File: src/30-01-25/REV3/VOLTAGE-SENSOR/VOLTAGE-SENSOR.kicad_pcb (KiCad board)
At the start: 2 copper layers, 90 x 85 mm, 83 parts, among them U1 LM324, U2 zmpt101b, U6 zmpt101b, U7 LM324, U8 zmpt101b, U9 LM324

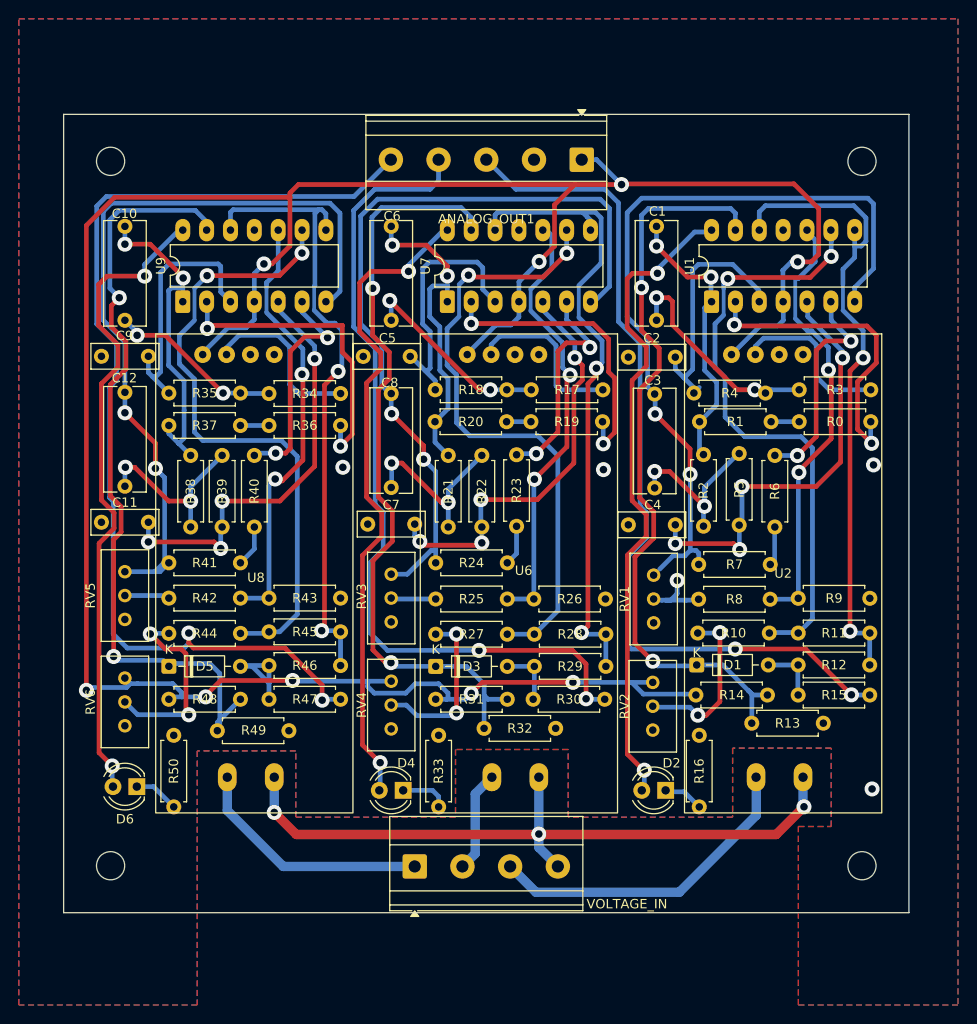
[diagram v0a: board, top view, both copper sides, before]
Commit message: Change: reading data by polling
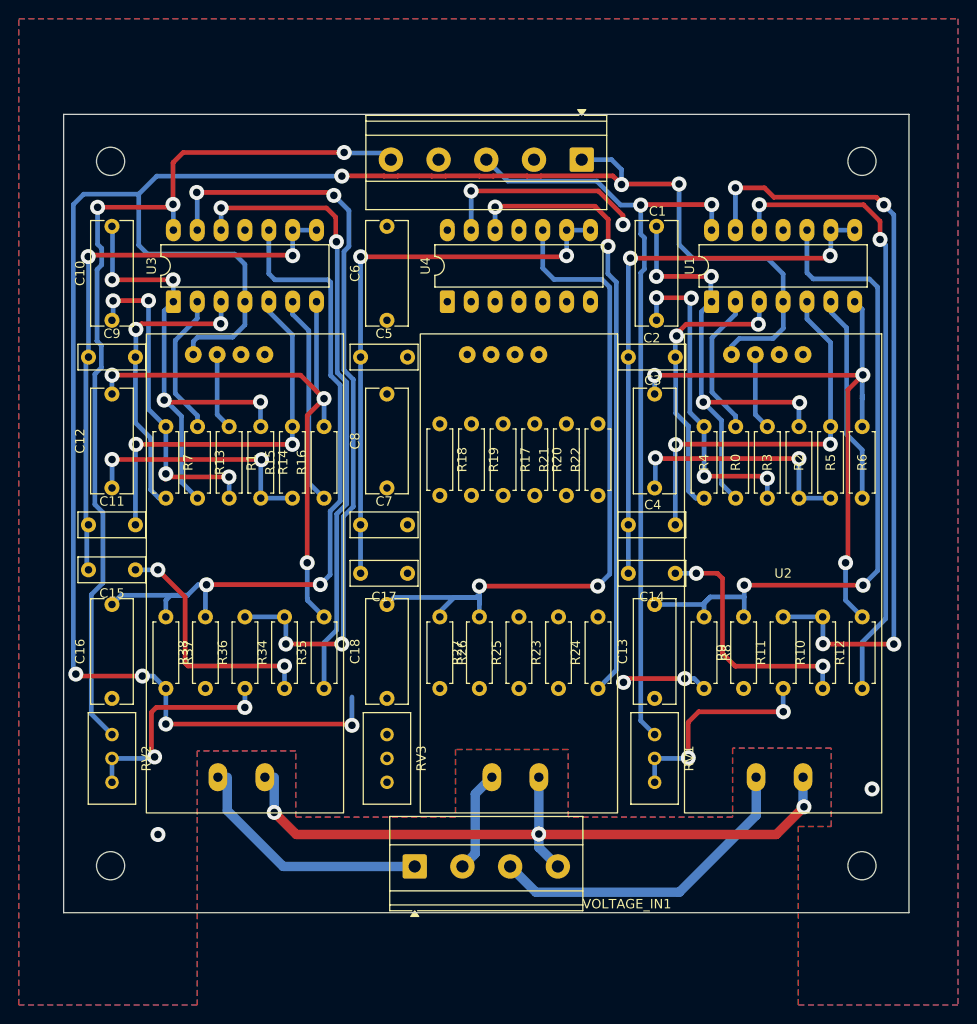
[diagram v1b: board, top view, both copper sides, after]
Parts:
- removed D1, D3, D5: 1N5711, Diode_THT:D_DO-35_SOD27_P7.62mm_Horizontal
- removed D2, D4, D6: LED, LED_THT:LED_D4.0mm
- removed R28, R29, R30, R39, R40, R41, R42, R43, R44, R45, R46, R47: 68k, Resistor_THT:R_Axial_DIN0207_L6.3mm_D2.5mm_P7.62mm_Horizontal
- removed R31, R48: 400, Resistor_THT:R_Axial_DIN0207_L6.3mm_D2.5mm_P7.62mm_Horizontal
- removed R32, R49: 420, Resistor_THT:R_Axial_DIN0207_L6.3mm_D2.5mm_P7.62mm_Horizontal
- removed R33, R50: 100, Resistor_THT:R_Axial_DIN0207_L6.3mm_D2.5mm_P7.62mm_Horizontal
- removed RV4, RV5, RV6: R_Potentiometer, Potentiometer_THT:Potentiometer_Bourns_3296W_Vertical
- removed U7, U9: LM324, Package_DIP:DIP-14_W7.62mm_LongPads
- added C13: 100nF, Capacitor_THT:C_Rect_L11.0mm_W4.3mm_P10.00mm_MKT, F.Cu at (157.7, 112.4)
- added C14: 1uF, Capacitor_THT:C_Rect_L7.0mm_W2.5mm_P5.00mm, F.Cu at (159.9, 99.0)
- added C15: 1uF, Capacitor_THT:C_Rect_L7.0mm_W2.5mm_P5.00mm, F.Cu at (102.4, 98.7)
- added C16: 100nF, Capacitor_THT:C_Rect_L11.0mm_W4.3mm_P10.00mm_MKT, F.Cu at (99.9, 112.4)
- added C17: 1uF, Capacitor_THT:C_Rect_L7.0mm_W2.5mm_P5.00mm, F.Cu at (131.4, 99.0)
- added C18: 100nF, Capacitor_THT:C_Rect_L11.0mm_W4.3mm_P10.00mm_MKT, F.Cu at (129.2, 112.4)
- added U3: LM324, Package_DIP:DIP-14_W7.62mm_LongPads, F.Cu at (106.5, 70.1)
- added U4: LM324, Package_DIP:DIP-14_W7.62mm_LongPads, F.Cu at (135.6, 70.1)
- R0, R19, R22, R6: value 68k -> 130k
- R10, R23, R34: value 68k -> 10k
- R11, R25, R36: value 68k -> 1k
- R12, R24, R35: value 68k -> 5.1k
- R13: value 420 -> 130k
- R14: value 400 -> 68k
- R16: value 100 -> 130k
- R26, R27, R37, R38, R8, R9: value 68k -> 100k
- RV1, RV2, RV3: value R_Potentiometer -> 10k
- moved R13 73.7 mm to (109.0, 83.4), turned to -90 degrees
- moved R7 66.0 mm to (105.7, 83.4), turned to -90 degrees
- moved R15 64.9 mm to (119.1, 91.0), turned to 90 degrees
- moved R14 61.0 mm to (115.8, 83.4), turned to -90 degrees
- moved RV2 58.5 mm to (99.9, 121.3), turned to -90 degrees
- moved R1 50.1 mm to (112.4, 83.4), turned to -90 degrees
- moved R16 47.3 mm to (122.5, 91.0), turned to 90 degrees
- moved R35 32.7 mm to (122.5, 111.3), turned to 90 degrees
- moved R34 32.0 mm to (118.3, 111.3), turned to 90 degrees
- moved R36 29.8 mm to (114.1, 111.3), turned to 90 degrees
- moved R23 25.3 mm to (147.5, 111.3), turned to 90 degrees
- moved R38 24.9 mm to (109.9, 111.3), turned to 90 degrees
- moved RV3 22.2 mm to (129.2, 121.3), turned to -90 degrees
- moved RV1 22.1 mm to (157.7, 121.3), turned to -90 degrees
- moved R37 20.4 mm to (105.7, 103.7), turned to -90 degrees
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- renumbered VOLTAGE_IN to VOLTAGE_IN1
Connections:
- C11 pad 1: GND -> VGND3
- C11 pad 2: Net-(U9B-+) -> Net-(U3B-+)
- C2 pad 1: GND -> VGND1
- C4 pad 1: GND -> VGND1
- C5 pad 1: GND -> VGND2
- C7 pad 1: GND -> VGND2
- C7 pad 2: Net-(U7B-+) -> Net-(U4B-+)
- C9 pad 1: GND -> VGND3
- C9 pad 2: Net-(U9A-+) -> Net-(U3A-+)
- R0 pad 2: Net-(R0-Pad2) -> Net-(C1-Pad2)
- R1 pad 1: Net-(C1-Pad2) -> OUT_S3
- R1 pad 2: Net-(R0-Pad2) -> Net-(C10-Pad1)
- R10 pad 1: Net-(R10-Pad1) -> Net-(C14-Pad1)
- R10 pad 2: Net-(U1C--) -> Net-(U1D--)
- R11 pad 1: Net-(U1D-+) -> Net-(R11-Pad1)
- R11 pad 2: Net-(U1C--) -> Net-(U1D--)
- R12 pad 1: Net-(D1-A) -> Net-(U1D-+)
- R12 pad 2: Net-(U1D-+) -> Net-(C3-Pad2)
- R13 pad 1: GND -> Net-(U3A--)
- R13 pad 2: Net-(D1-K) -> Net-(C10-Pad2)
- R14 pad 1: Net-(D1-K) -> Net-(C10-Pad2)
- R14 pad 2: 5V -> Net-(C12-Pad1)
- R15 pad 1: SIGNAL_OUT1 -> Net-(C12-Pad1)
- R15 pad 2: Net-(D1-A) -> Net-(U3B-+)
- R16 pad 1: GND -> Net-(U3B--)
- R16 pad 2: Net-(D2-K) -> Net-(C12-Pad2)
- R19 pad 2: Net-(R19-Pad2) -> Net-(C6-Pad2)
- R20 pad 2: Net-(R19-Pad2) -> Net-(C8-Pad1)
- R21 pad 1: Net-(C6-Pad2) -> Net-(C8-Pad1)
- R21 pad 2: Net-(C8-Pad1) -> Net-(U4B-+)
- R22 pad 1: Net-(C8-Pad1) -> Net-(U4B--)
- R22 pad 2: Net-(U7B-+) -> Net-(C8-Pad2)
- R23 pad 2: Net-(R23-Pad2) -> Net-(U4D--)
- R24 pad 1: Net-(R23-Pad2) -> Net-(U4D-+)
- R25 pad 2: Net-(U7C-+) -> Net-(U4D--)
- R26 pad 1: GND -> Net-(U4C-+)
- R26 pad 2: Net-(U7C-+) -> 5V
- R27 pad 1: Net-(R27-Pad1) -> GND
- R27 pad 2: Net-(U7C--) -> Net-(U4C-+)
- R34 pad 1: OUT_S3 -> Net-(C15-Pad1)
- R34 pad 2: Net-(C10-Pad1) -> Net-(U3D--)
- R35 pad 1: Net-(C10-Pad1) -> Net-(U3D-+)
- R35 pad 2: Net-(U9A-+) -> Net-(C12-Pad2)
- R36 pad 1: Net-(U9A--) -> Net-(R36-Pad1)
- R36 pad 2: Net-(R36-Pad2) -> Net-(U3D--)
- R37 pad 1: Net-(C10-Pad2) -> Net-(U3C-+)
- R37 pad 2: Net-(R36-Pad2) -> 5V
- R38 pad 1: Net-(C10-Pad2) -> GND
- R38 pad 2: Net-(C12-Pad1) -> Net-(U3C-+)
- R6 pad 2: Net-(R6-Pad2) -> Net-(C3-Pad2)
- R7 pad 1: Net-(R6-Pad2) -> Net-(C10-Pad1)
- R7 pad 2: Net-(C3-Pad2) -> Net-(U3A-+)
- R8 pad 1: Net-(R8-Pad1) -> Net-(U1C-+)
- R8 pad 2: Net-(U1C-+) -> 5V
- RV1 pad 1: Net-(C3-Pad2) -> Net-(R11-Pad1)
- RV1 pad 2: Net-(R8-Pad1) -> Net-(R11-Pad1)
- RV1 pad 3: GND -> SIGNAL_OUT1
- RV2 pad 1: 5V -> Net-(R36-Pad1)
- RV2 pad 2: Net-(R10-Pad1) -> Net-(R36-Pad1)
- RV2 pad 3: GND -> SIGNAL_OUT3
- RV3 pad 1: Net-(C8-Pad2) -> Net-(R25-Pad1)
- RV3 pad 3: GND -> SIGNAL_OUT2
- U1 pad 13: Net-(D1-K) -> Net-(U1D--)
- U1 pad 14: Net-(D2-A) -> SIGNAL_OUT1
- U1 pad 8: Net-(U1D-+) -> VGND1
- U1 pad 9: Net-(U1C--) -> VGND1
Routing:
- net SIGNAL_OUT2: track 89.7 -> 0.00 mm, vias 2 -> 0
- net Net-(C8-Pad2): track 84.8 -> 0.00 mm, vias 2 -> 0
- net Net-(D5-K): track 84.4 -> 0.00 mm, vias 2 -> 0
- net Net-(U1D--): track 0.00 -> 82.9 mm, vias 0 -> 4
- net Net-(D3-K): track 82.2 -> 0.00 mm, vias 2 -> 0
- net Net-(U3D--): track 0.00 -> 81.5 mm, vias 0 -> 4
- net Net-(D1-K): track 80.0 -> 0.00 mm, vias 2 -> 0
- net Net-(U4C-+): track 0.00 -> 78.0 mm, vias 0 -> 2
- net Net-(U3C-+): track 0.00 -> 75.9 mm, vias 0 -> 2
- net Net-(D4-A): track 70.0 -> 0.00 mm, vias 2 -> 0
- net Net-(D2-A): track 69.6 -> 0.00 mm, vias 2 -> 0
- net Net-(D6-A): track 69.0 -> 0.00 mm, vias 2 -> 0
- net Net-(U7D-+): track 68.7 -> 0.00 mm, vias 2 -> 0
- net Net-(U9D-+): track 68.0 -> 0.00 mm, vias 2 -> 0
- net Net-(U9C--): track 67.8 -> 0.00 mm, vias 2 -> 0
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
